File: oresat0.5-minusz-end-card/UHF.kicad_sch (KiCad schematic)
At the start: 1 part

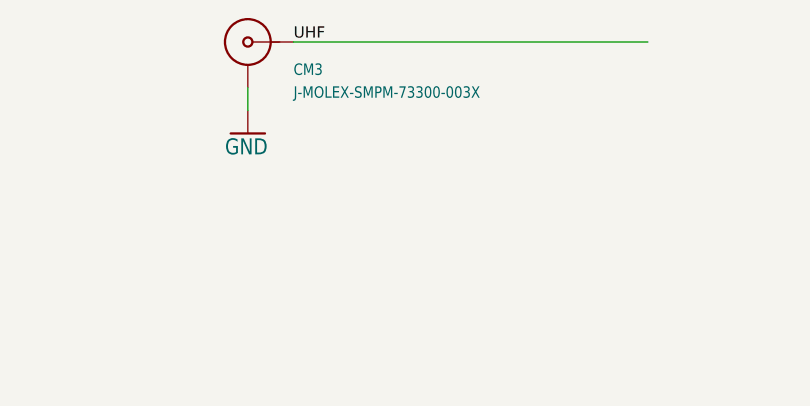
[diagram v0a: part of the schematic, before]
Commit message: Updated -Z end card and replaced eagle imported libraries with kicad libraries
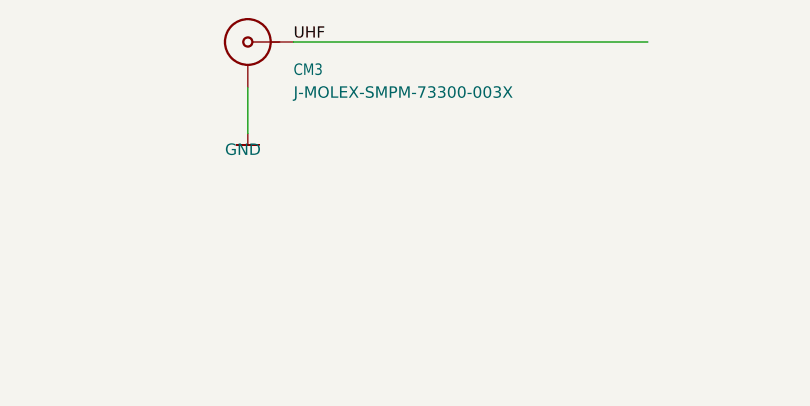
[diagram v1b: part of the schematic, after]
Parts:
- CM3: footprint oresat-footprints:J-MOLEX-SMPM-073300-003X -> oresat-connectors:J-MOLEX-SMPM-073300-003X; symbol OreSat-j-molex-smpm-73300-003x:J-MOLEX-SMPM-73300-003X -> oresat-connectors:J-MOLEX-SMPM-73300-003X
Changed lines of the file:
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@@
     (rev "1.0")
   )
-  (wire (pts (xy 57.15 139.7) (xy 57.15 137.16))
+  (wire (pts (xy 57.15 137.16) (xy 57.15 142.24))
     (stroke (width 0) (type default) (color 0 0 0 0))
   )
@@
     (effects (font (size 1.2446 1.2446)) (justify left bottom))
   )
-  (symbol (lib_id "plusz-end-card-with-turnstile-eagle-import:GND") (at 57.15 142.24 0) (unit 1)
+  (symbol (lib_id "oresat-power:GND") (at 57.15 142.24 0) (unit 1)
     (in_bom yes) (on_board yes)
     (property "Reference" "#GND011" (id 0) (at 57.15 142.24 0)
@@
     )
     (property "Value" "GND" (id 1) (at 54.61 144.78 0)
-      (effects (font (size 1.778 1.5113)) (justify left bottom))
+      (effects (font (size 1.27 1.27)) (justify left bottom))
     )
     (property "Footprint" "plusz-end-card-with-turnstile:" (id 2) (at 57.15 142.24 0)
@@
     (pin "1")
   )
-  (symbol (lib_id "OreSat-j-molex-smpm-73300-003x:J-MOLEX-SMPM-73300-003X") (at 57.15 132.08 0) (unit 1)
+  (symbol (lib_id "oresat-connectors:J-MOLEX-SMPM-73300-003X") (at 57.15 132.08 0) (unit 1)
     (in_bom yes) (on_board yes)
     (property "Reference" "CM3" (id 0) (at 62.23 135.89 0)
@@
     )
     (property "Value" "J-MOLEX-SMPM-73300-003X" (id 1) (at 62.23 138.43 0)
-      (effects (font (size 1.27 1.0795)) (justify left bottom))
+      (effects (font (size 1.27 1.27)) (justify left bottom))
     )
-    (property "Footprint" "oresat-footprints:J-MOLEX-SMPM-073300-003X" (id 2) (at 57.15 132.08 0)
+    (property "Footprint" "oresat-connectors:J-MOLEX-SMPM-073300-003X" (id 2) (at 57.15 132.08 0)
       (effects (font (size 1.27 1.27)) hide)
     )

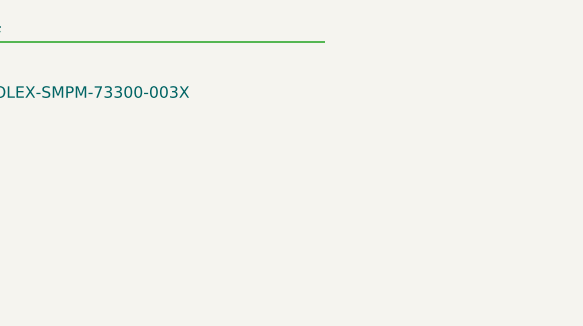
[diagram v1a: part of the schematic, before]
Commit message: -Z end card design review changes, and added antenna feeds
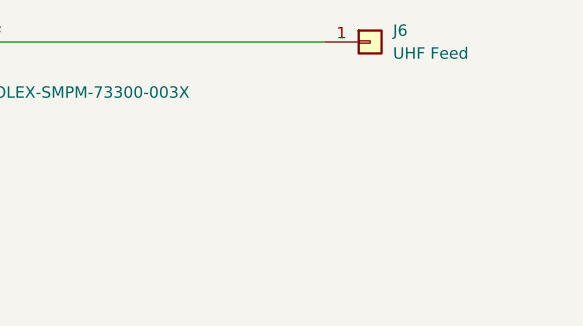
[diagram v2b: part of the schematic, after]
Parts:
- added J6: UHF Feed, Connector_Pin:Pin_D1.0mm_L10.0mm, symbol Connector_Generic:Conn_01x01
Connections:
- net UHF: now also J6.1 (Pin_1)
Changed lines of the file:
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@@
     (effects (font (size 1.2446 1.2446)) (justify left bottom))
+  )
+  (symbol (lib_id "Connector_Generic:Conn_01x01") (at 106.68 132.08 0) (unit 1)
+    (in_bom yes) (on_board yes) (fields_autoplaced)
+    (property "Reference" "J6" (id 0) (at 109.22 130.8099 0)
+      (effects (font (size 1.27 1.27)) (justify left))
+    )
+    (property "Value" "UHF Feed" (id 1) (at 109.22 133.3499 0)
+      (effects (font (size 1.27 1.27)) (justify left))
+    )
+    (property "Footprint" "Connector_Pin:Pin_D1.0mm_L10.0mm" (id 2) (at 106.68 132.08 0)
+      (effects (font (size 1.27 1.27)) hide)
+    )
+    (property "Datasheet" "~" (id 3) (at 106.68 132.08 0)
+      (effects (font (size 1.27 1.27)) hide)
+    )
+    (pin "1")
   )
   (symbol (lib_id "oresat-power:GND") (at 57.15 142.24 0) (unit 1)

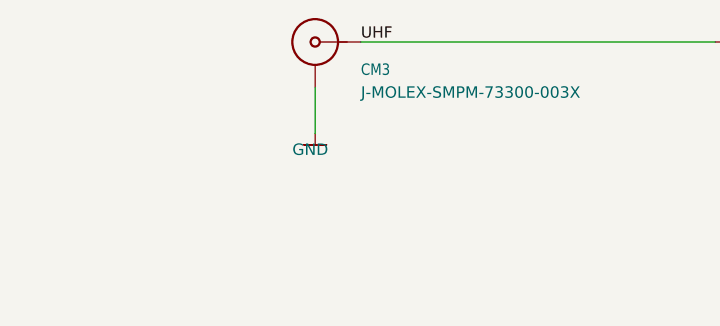
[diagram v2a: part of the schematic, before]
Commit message: Updated OreSat 0.5 end card board outlines and mounting holes, and fixed KiCad library warnings
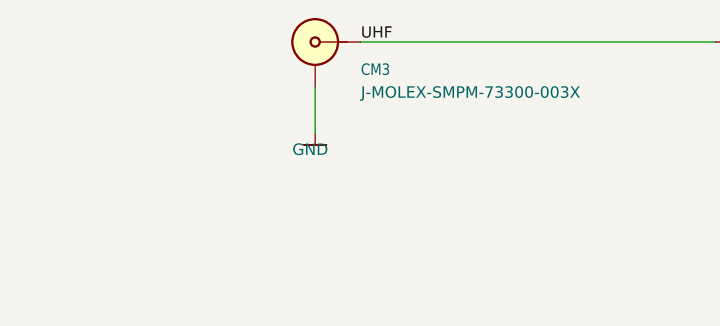
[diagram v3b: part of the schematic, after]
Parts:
- CM3: footprint oresat-connectors:J-MOLEX-SMPM-073300-003X -> oresat-connectors:J-MOLEX-SMPM-073300-002X; symbol oresat-connectors:J-MOLEX-SMPM-73300-003X -> oresat-connectors:J-MOLEX-SMPM-73300-002X
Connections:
- net GND: now also CM3.SHLD; no longer CM3.GND (SHIELD3)
- net UHF: now also CM3.SIG; no longer CM3.RF (CENTER)
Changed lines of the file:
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@@
-(kicad_sch (version 20211123) (generator eeschema)
+(kicad_sch (version 20230121) (generator eeschema)
   (paper "USLedger")
   (title_block
@@
   )
   (wire (pts (xy 57.15 137.16) (xy 57.15 142.24))
-    (stroke (width 0) (type default) (color 0 0 0 0))
+    (stroke (width 0) (type default))
   )
   (wire (pts (xy 101.6 132.08) (xy 62.23 132.08))
-    (stroke (width 0) (type default) (color 0 0 0 0))
+    (stroke (width 0) (type default))
   )
-  (text "UHF Feed System (436.5 MHz)" (at 24.13 247.65 180)
+  (text "UHF Feed System (436.5 MHz)" (at 24.13 247.65 0)
     (effects (font (size 4.572 3.8862)) (justify left bottom))
   )
-  (label "UHF" (at 62.23 132.08 0)
+  (label "UHF" (at 62.23 132.08 0) (fields_autoplaced)
     (effects (font (size 1.2446 1.2446)) (justify left bottom))
   )
   (symbol (lib_id "Connector_Generic:Conn_01x01") (at 106.68 132.08 0) (unit 1)
-    (in_bom yes) (on_board yes) (fields_autoplaced)
-    (property "Reference" "J6" (id 0) (at 109.22 130.8099 0)
+    (in_bom yes) (on_board yes) (dnp no) (fields_autoplaced)
+    (property "Reference" "J6" (at 109.22 130.8099 0)
       (effects (font (size 1.27 1.27)) (justify left))
     )
-    (property "Value" "UHF Feed" (id 1) (at 109.22 133.3499 0)
+    (property "Value" "UHF Feed" (at 109.22 133.3499 0)
       (effects (font (size 1.27 1.27)) (justify left))
     )
-    (property "Footprint" "Connector_Pin:Pin_D1.0mm_L10.0mm" (id 2) (at 106.68 132.08 0)
+    (property "Footprint" "Connector_Pin:Pin_D1.0mm_L10.0mm" (at 106.68 132.08 0)
       (effects (font (size 1.27 1.27)) hide)
     )
-    (property "Datasheet" "~" (id 3) (at 106.68 132.08 0)
+    (property "Datasheet" "~" (at 106.68 132.08 0)
       (effects (font (size 1.27 1.27)) hide)
     )
     (pin "1")
+    (instances
+      (project "oresat0.5-minusz-end-card"
+        (path "/f7595184-4323-4ed9-b19e-5e32e3c6e76f/7efb4e63-9d62-4a45-8323-bca1b123bd45"
+          (reference "J6") (unit 1)
+        )
+      )
+    )
   )
   (symbol (lib_id "oresat-power:GND") (at 57.15 142.24 0) (unit 1)
-    (in_bom yes) (on_board yes)
-    (property "Reference" "#GND011" (id 0) (at 57.15 142.24 0)
+    (in_bom yes) (on_board yes) (dnp no)
+    (property "Reference" "#GND011" (at 57.15 142.24 0)
       (effects (font (size 1.27 1.27)) hide)
     )
-    (property "Value" "GND" (id 1) (at 54.61 144.78 0)
+    (property "Value" "GND" (at 54.61 144.78 0)
       (effects (font (size 1.27 1.27)) (justify left bottom))
     )
-    (property "Footprint" "plusz-end-card-with-turnstile:" (id 2) (at 57.15 142.24 0)
+    (property "Footprint" "plusz-end-card-with-turnstile:" (at 57.15 142.24 0)
       (effects (font (size 1.27 1.27)) hide)
     )
-    (property "Datasheet" "" (id 3) (at 57.15 142.24 0)
+    (property "Datasheet" "" (at 57.15 142.24 0)
       (effects (font (size 1.27 1.27)) hide)
     )
     (pin "1")
+    (instances
+      (project "oresat0.5-minusz-end-card"
+        (path "/f7595184-4323-4ed9-b19e-5e32e3c6e76f/7efb4e63-9d62-4a45-8323-bca1b123bd45"
+          (reference "#GND011") (unit 1)
+        )
+      )
+    )
   )
-  (symbol (lib_id "oresat-connectors:J-MOLEX-SMPM-73300-003X") (at 57.15 132.08 0) (unit 1)
-    (in_bom yes) (on_board yes)
-    (property "Reference" "CM3" (id 0) (at 62.23 135.89 0)
+  (symbol (lib_id "oresat-connectors:J-MOLEX-SMPM-73300-002X") (at 57.15 132.08 0) (unit 1)
+    (in_bom yes) (on_board yes) (dnp no)
+    (property "Reference" "CM3" (at 62.23 135.89 0)
       (effects (font (size 1.27 1.0795)) (justify left bottom))
     )
-    (property "Value" "J-MOLEX-SMPM-73300-003X" (id 1) (at 62.23 138.43 0)
+    (property "Value" "J-MOLEX-SMPM-73300-003X" (at 62.23 138.43 0)
       (effects (font (size 1.27 1.27)) (justify left bottom))
     )
-    (property "Footprint" "oresat-connectors:J-MOLEX-SMPM-073300-003X" (id 2) (at 57.15 132.08 0)
+    (property "Footprint" "oresat-connectors:J-MOLEX-SMPM-073300-002X" (at 57.15 125.73 0)
       (effects (font (size 1.27 1.27)) hide)
     )
-    (property "Datasheet" "" (id 3) (at 57.15 132.08 0)
+    (property "Datasheet" "https://tools.molex.com/pdm_docs/sd/733000020_sd.pdf" (at 57.15 123.19 0)
       (effects (font (size 1.27 1.27)) hide)
     )
-    (pin "GND")
-    (pin "RF")
+    (pin "SHLD")
+    (pin "SIG")
+    (instances
+      (project "oresat0.5-minusz-end-card"
+        (path "/f7595184-4323-4ed9-b19e-5e32e3c6e76f/7efb4e63-9d62-4a45-8323-bca1b123bd45"
+          (reference "CM3") (unit 1)
+        )
+      )
+    )
   )
 )

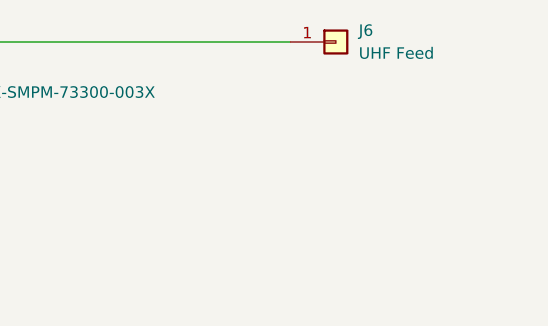
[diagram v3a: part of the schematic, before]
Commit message: Updated -Z end card and DXF
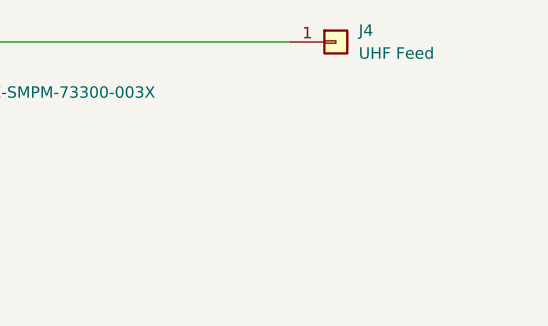
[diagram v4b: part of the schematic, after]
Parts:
- renumbered J6 to J4
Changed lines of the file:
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@@
   (symbol (lib_id "Connector_Generic:Conn_01x01") (at 106.68 132.08 0) (unit 1)
     (in_bom yes) (on_board yes) (dnp no) (fields_autoplaced)
-    (property "Reference" "J6" (at 109.22 130.8099 0)
+    (property "Reference" "J4" (at 109.22 130.81 0)
       (effects (font (size 1.27 1.27)) (justify left))
     )
-    (property "Value" "UHF Feed" (at 109.22 133.3499 0)
+    (property "Value" "UHF Feed" (at 109.22 133.35 0)
       (effects (font (size 1.27 1.27)) (justify left))
     )
@@
       (project "oresat0.5-minusz-end-card"
         (path "/f7595184-4323-4ed9-b19e-5e32e3c6e76f/7efb4e63-9d62-4a45-8323-bca1b123bd45"
-          (reference "J6") (unit 1)
+          (reference "J4") (unit 1)
         )
       )
